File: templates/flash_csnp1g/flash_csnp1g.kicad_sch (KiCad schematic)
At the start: 3 parts

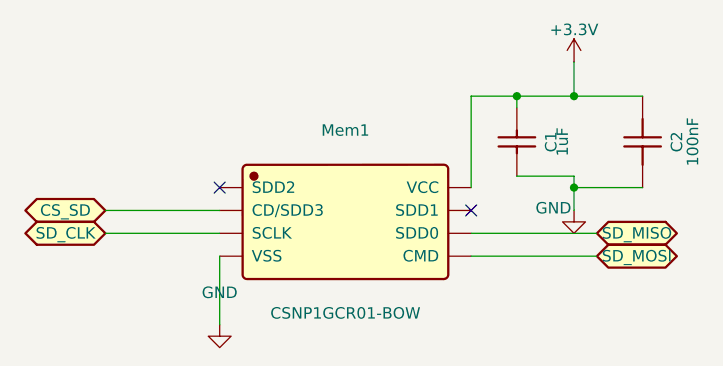
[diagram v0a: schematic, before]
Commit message: Fix ESP32 GPIO wiring and flash chip select separation
- Add CS_FLASH port symbol to Ports.kicad_sym
- Map 9 ESP32 GPIO to ports: I2S (IO4-IO6), AMP_EN (IO7),
  SPI (IO15-IO18), CS_FLASH (IO8)
- Change flash template from CS_SD to CS_FLASH for separate
  chip select lines between flash and SD card
- Regenerate schematic with all signal connections verified

Co-Authored-By: Claude Opus 4.6 <noreply@anthropic.com>
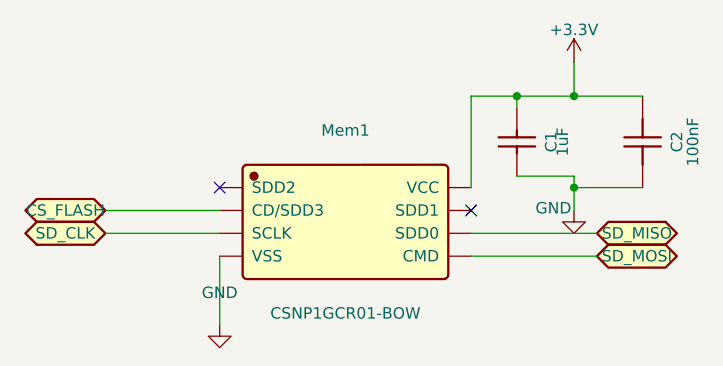
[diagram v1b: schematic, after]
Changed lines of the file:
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@@
 	)
 	(symbol
-		(lib_id "Ports:CS_SD")
+		(lib_id "Ports:CS_FLASH")
 		(at 120.65 99.06 0)
 		(unit 1)
@@
 			)
 		)
-		(property "Value" "CS_SD"
+		(property "Value" "CS_FLASH"
 			(at 118.75 99.06 0)
 			(effects
